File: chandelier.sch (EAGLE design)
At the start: 18 parts, among them IC1 NDC7002N-DUAL-MOS-N, IC2 NDC7002N-DUAL-MOS-N, IC3 NDC7002N-DUAL-MOS-N, IC4 NDC7002N-DUAL-MOS-N, IC9 74595, J1 HEADER, J10 HEADER, J2 HEADER, J3 HEADER, J4 HEADER, J5 HEADER, J6 HEADER, J7 HEADER, J8 HEADER, J9 HEADER

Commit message: adding uncommitted things
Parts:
- added C1: 1uF, SparkFun-Capacitors:CAP0805
- renumbered IC9 to IC5, U$1 to IC6
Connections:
- removed net VCC: JP1.6, JP2.6
- net GND: now also C1.2
- net VCC3V3: now also C1.1, JP1.6, JP2.6

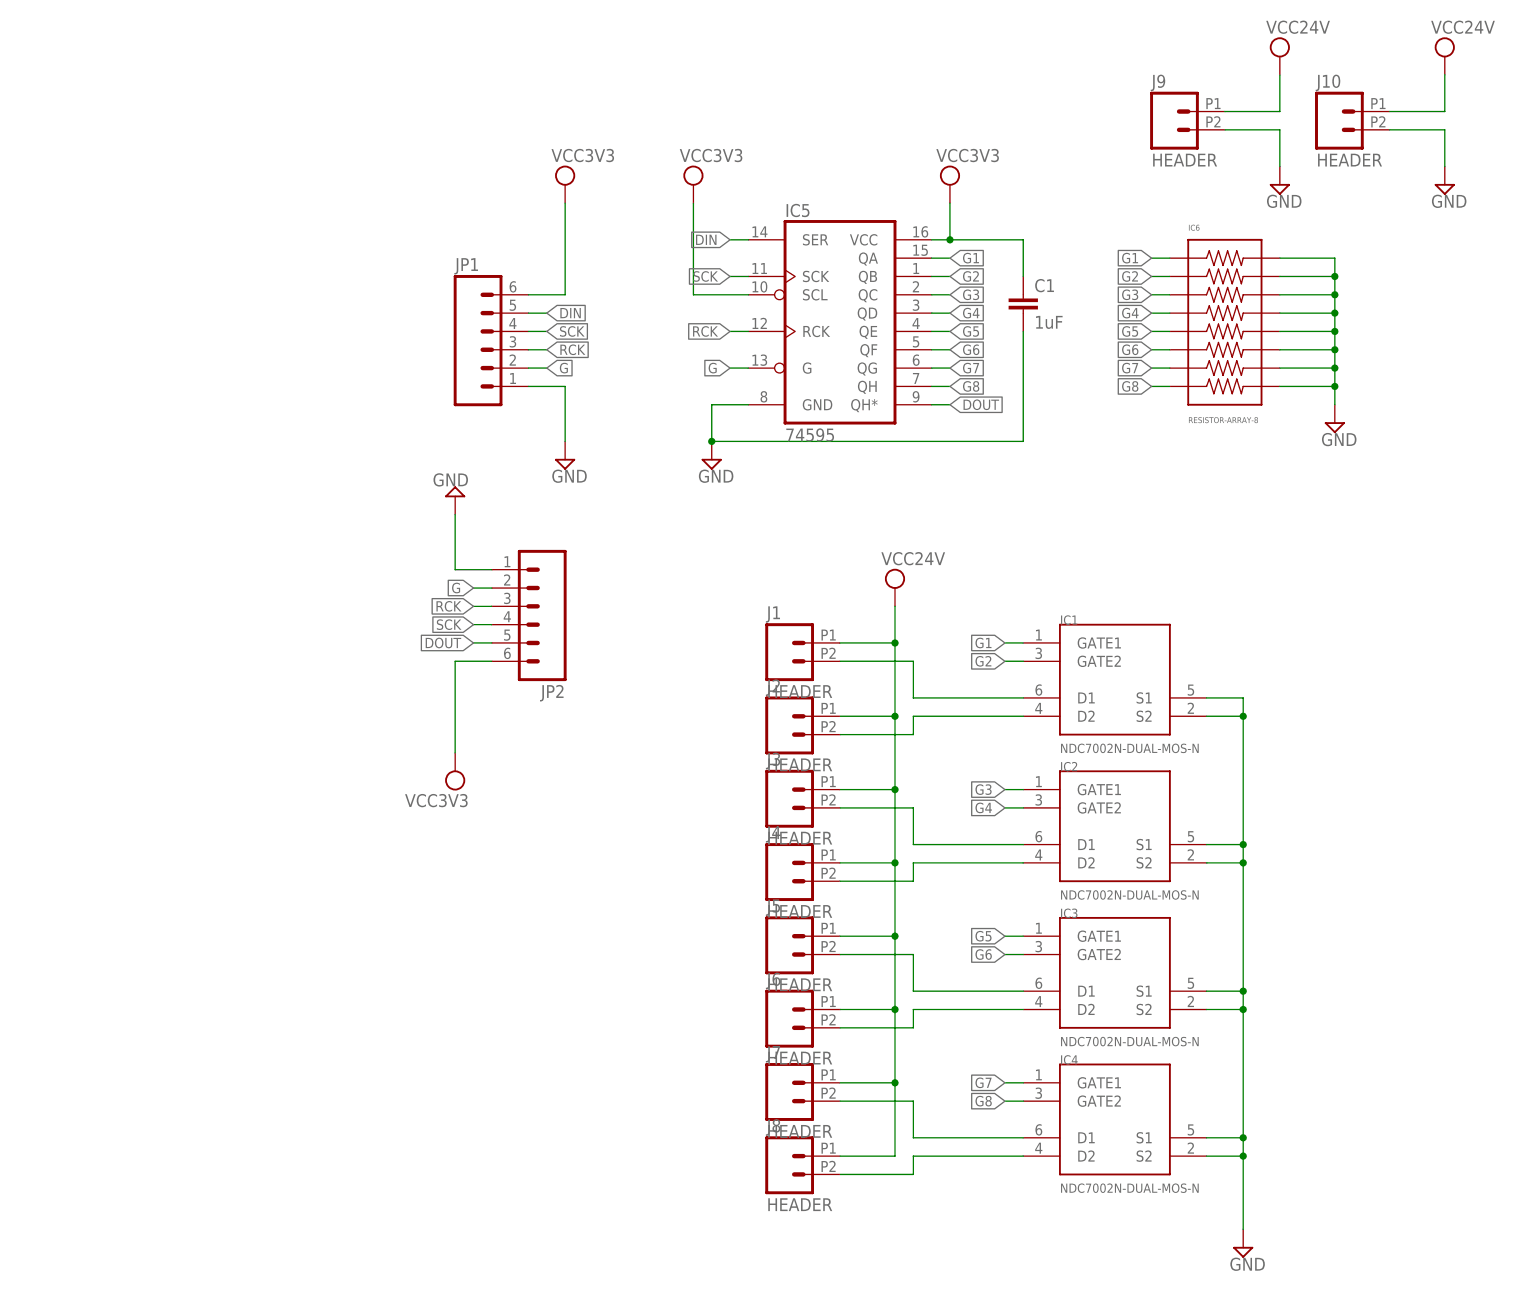
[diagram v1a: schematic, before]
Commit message: added bom
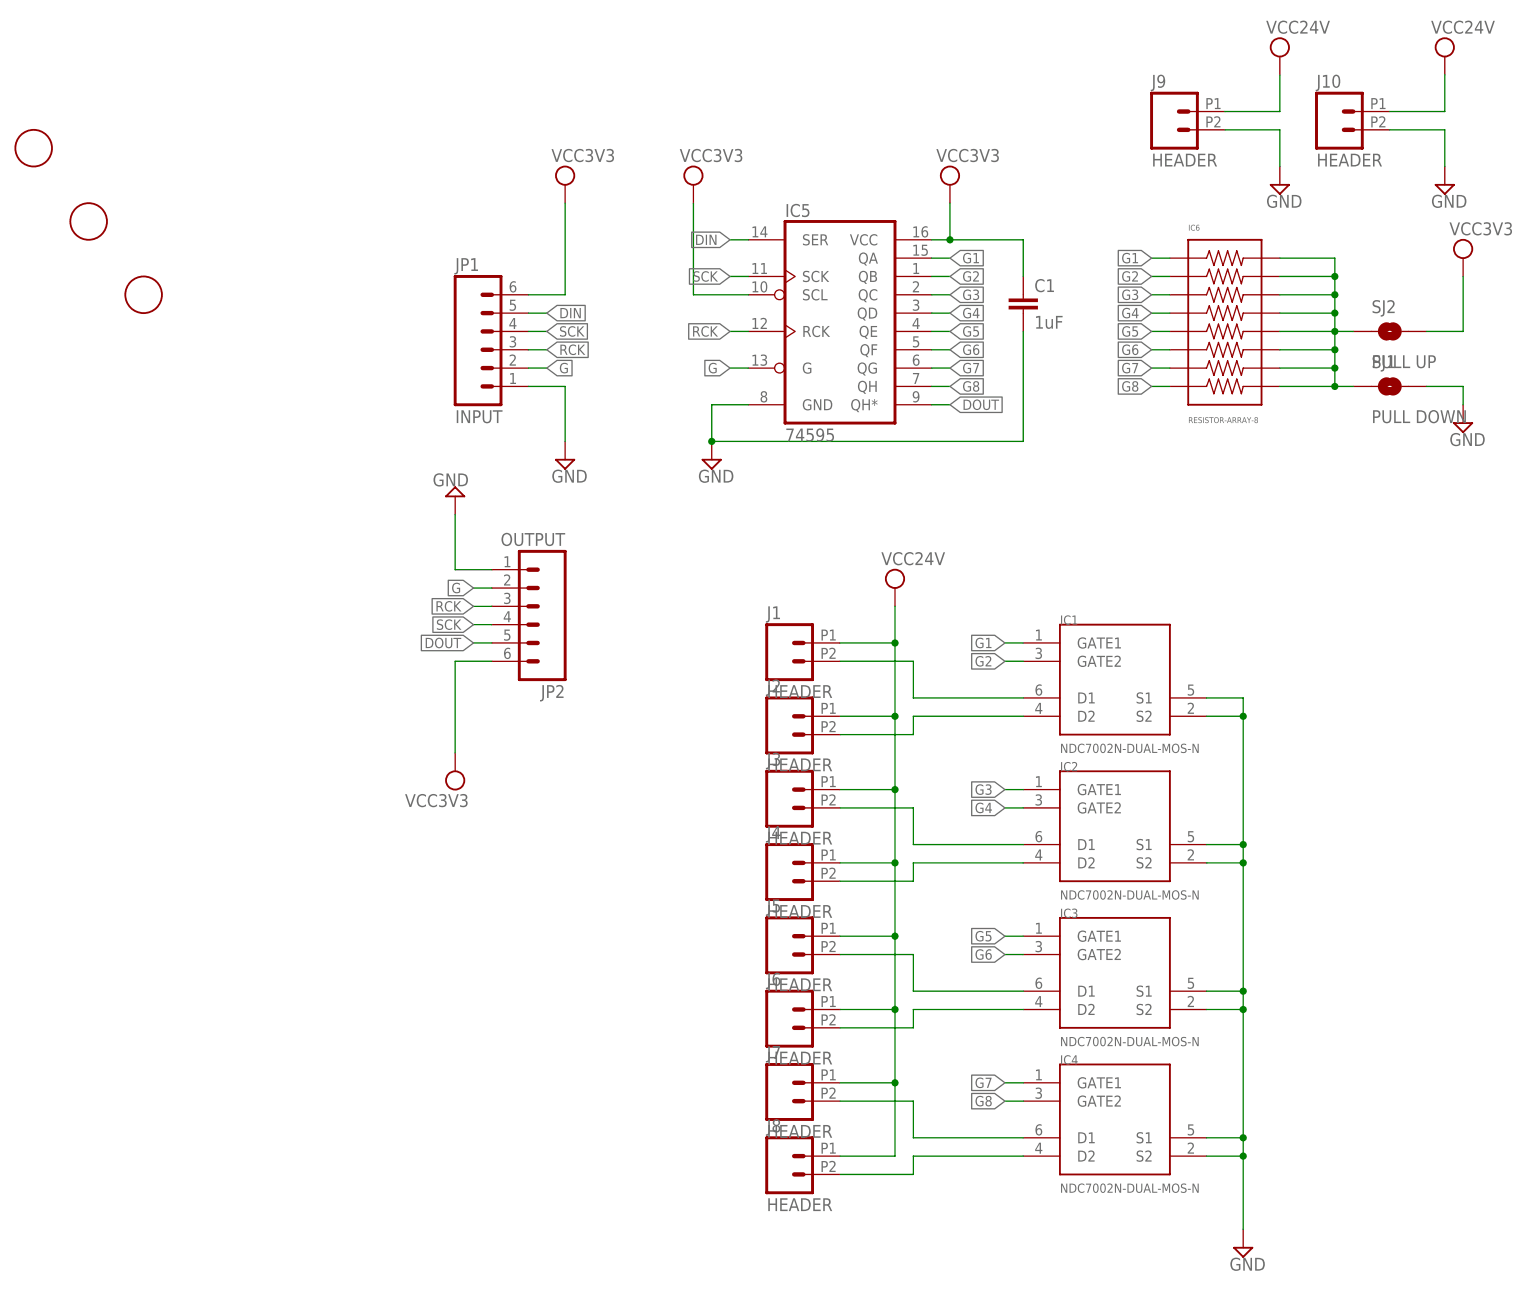
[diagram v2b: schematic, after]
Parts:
- added SJ1: PULL DOWN, SparkFun-Passives:SOLDERJUMPERTRACE
- added SJ2: PULL UP, SparkFun-Passives:SOLDERJUMPERNO
- added U$1, U$4, U$5: FIDUCIAL, adafruit:FIDUCIAL
- C1: PARTNO (none) -> CL21B105KOFNNNE
- IC1, IC2, IC3, IC4: PARTNO (none) -> NDC7002N
- IC5: PARTNO (none) -> 74VHC595MTCX
- IC6: PARTNO (none) -> CAY16-103J8LF
- JP1: value (none) -> INPUT
- JP2: value (none) -> OUTPUT
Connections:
- new net N$9: IC6.1, IC6.11, IC6.13, IC6.15, IC6.3, IC6.5, IC6.7, IC6.9, SJ1.1, SJ2.1
- net GND: now also SJ1.2; no longer IC6.1, IC6.11, IC6.13, IC6.15, IC6.3, IC6.5, IC6.7, IC6.9
- net VCC3V3: now also SJ2.2

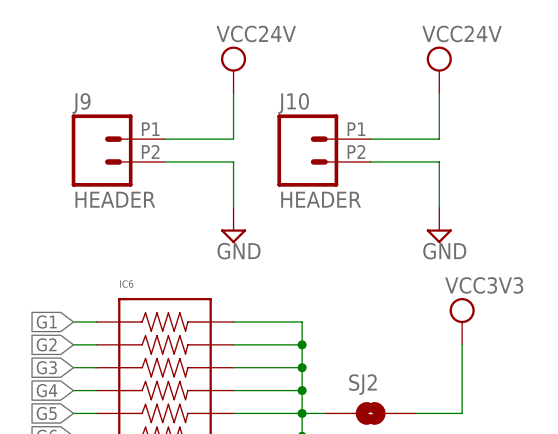
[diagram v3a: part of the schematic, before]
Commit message: fixed trace issues for 1.3
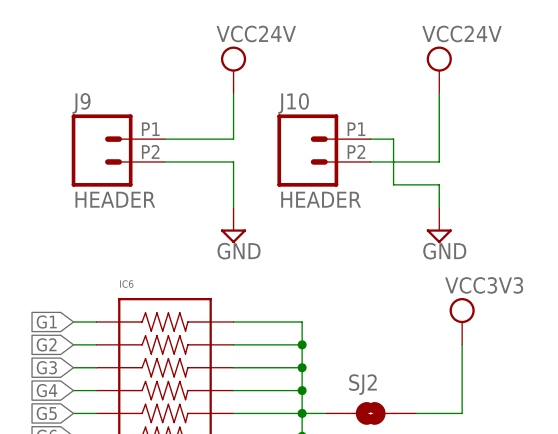
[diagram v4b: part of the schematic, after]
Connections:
- net GND: now also J10.2; no longer J10.1
- net VCC24V: now also J10.1; no longer J10.2
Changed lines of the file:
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@@
 <?xml version="1.0" encoding="utf-8"?>
 <!DOCTYPE eagle SYSTEM "eagle.dtd">
-<eagle version="6.5.0">
+<eagle version="6.4">
 <drawing>
 <settings>
@@
 </variantdefs>
 <classes>
-<class number="0" name="default" width="0.1524" drill="0.3302">
+<class number="0" name="default" width="0.1524" drill="0.381">
 <clearance class="0" value="0.1524"/>
 </class>
-<class number="1" name="power" width="0.254" drill="0.3302">
+<class number="1" name="power" width="0.254" drill="0.381">
 <clearance class="1" value="0.1524"/>
 </class>
@@
 </segment>
 <segment>
-<pinref part="J10" gate="G$1" pin="1"/>
-<pinref part="SUPPLY7" gate="GND" pin="GND"/>
-<wire x1="55.88" y1="198.12" x2="63.5" y2="198.12" width="0.1524" layer="91"/>
-<wire x1="63.5" y1="198.12" x2="63.5" y2="193.04" width="0.1524" layer="91"/>
-</segment>
-<segment>
 <pinref part="SJ1" gate="1" pin="2"/>
 <pinref part="SUPPLY3" gate="GND" pin="GND"/>
 <wire x1="60.96" y1="162.56" x2="66.04" y2="162.56" width="0.1524" layer="91"/>
 <wire x1="66.04" y1="162.56" x2="66.04" y2="160.02" width="0.1524" layer="91"/>
+</segment>
+<segment>
+<pinref part="J10" gate="G$1" pin="2"/>
+<wire x1="55.88" y1="200.66" x2="58.42" y2="200.66" width="0.1524" layer="91"/>
+<wire x1="58.42" y1="200.66" x2="58.42" y2="195.58" width="0.1524" layer="91"/>
+<wire x1="58.42" y1="195.58" x2="63.5" y2="195.58" width="0.1524" layer="91"/>
+<pinref part="SUPPLY7" gate="GND" pin="GND"/>
+<wire x1="63.5" y1="195.58" x2="63.5" y2="193.04" width="0.1524" layer="91"/>
 </segment>
 </net>
@@
 </segment>
 <segment>
-<pinref part="J10" gate="G$1" pin="2"/>
+<pinref part="J10" gate="G$1" pin="1"/>
 <pinref part="\VAL6" gate="G$1" pin="VCC"/>
-<wire x1="55.88" y1="200.66" x2="63.5" y2="200.66" width="0.1524" layer="91"/>
-<wire x1="63.5" y1="200.66" x2="63.5" y2="205.74" width="0.1524" layer="91"/>
+<wire x1="55.88" y1="198.12" x2="63.5" y2="198.12" width="0.1524" layer="91"/>
+<wire x1="63.5" y1="198.12" x2="63.5" y2="205.74" width="0.1524" layer="91"/>
 </segment>
 </net>
